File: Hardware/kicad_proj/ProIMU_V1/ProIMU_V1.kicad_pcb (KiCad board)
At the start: 2 copper layers, 50 x 50 mm, 66 parts, among them IC1 MP2731GQC-0000-Z, J1 Conn_02x03_Counter_Clockwise, J4 502570-0893, Q1 2SC4213, U1 ADM101E, U10 STM32F412RETx, U2 TJA1051T-3, U3 LTC2942-1, U4 AIR602, U5 BMP280, U6 MPU-9250, U7 TPS54308, U9 L80-M39

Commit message: Updated Schematic and Layout
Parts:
- C1, C17, C18, C19, C20, C21, C22, C4, U1, U2: moved to F.Cu
- C5, R1, R2: moved to B.Cu
- moved IC1 173.3 mm to (47.5, 85.5)
- moved C12 169.9 mm to (79.1, 88.4)
- moved C26 169.9 mm to (53.7, 97.1)
- moved C6 169.9 mm to (96.4, 57.3)
- moved D2 169.9 mm to (56.4, 87.8)
- moved R14 169.9 mm to (48.8, 101.1)
- moved R15 169.9 mm to (53.4, 93.2)
- moved BAT1 169.9 mm to (49.5, 92.5)
- moved C10 169.9 mm to (86.1, 70.9)
- moved C11 169.9 mm to (94.0, 59.2)
- moved C14 169.9 mm to (75.8, 90.4)
- moved C16 169.9 mm to (124.5, 56.5)
- moved C2 169.9 mm to (76.2, 78.2)
- moved C23 169.9 mm to (56.6, 92.1)
- moved C24 169.9 mm to (60.0, 87.6)
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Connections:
- C5 pad 1: GND -> Net-(CAN1-Pad1)
- CAN1 pad 1: GND -> Net-(CAN1-Pad1)
- CAN1 pad 4: GND -> Net-(CAN1-Pad1)
- U10 pad 11: /MCU/GPS_RESET -> unconnected-(U10-Pad11)
- U10 pad 28: unconnected-(U10-Pad28) -> /MCU/GPS_RESET
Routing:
- net /MCU/CAN_SHUTDOWN: track 0.00 -> 23.5 mm, vias 0 -> 1
- net /MCU/WIFI_UART2_TX: track 0.00 -> 23.3 mm, vias 0 -> 1
- net /MCU/WIFI_UART2_RX: track 0.00 -> 21.9 mm, vias 0 -> 1
- net Net-(CAN1-Pad1): track 0.00 -> 18.7 mm, vias 0 -> 2
- net /MCU/SDCARD_DET_LEVEL: track 0.00 -> 18.2 mm
- net /MCU/GPS_RESET: track 0.00 -> 18.0 mm, vias 0 -> 1
- net /MCU/WIFI_RESET: track 0.00 -> 17.7 mm, vias 0 -> 1
- net /MCU/CAN1_RX: track 0.00 -> 16.6 mm, vias 0 -> 1
- net /MCU/MPU9250_SPI1_nCSS: track 0.00 -> 12.7 mm, vias 0 -> 1
- net /MCU/MPU9250_SPI1_SCK: track 0.00 -> 12.5 mm, vias 0 -> 1
- net /MCU/MPU9250_SPI1_MISO: track 0.00 -> 12.3 mm, vias 0 -> 1
- net /MCU/CAN1_TX: track 0.00 -> 11.5 mm, vias 0 -> 1
- net Net-(C21-Pad2): track 11.5 -> 0.00 mm, vias 2 -> 0
- net /MCU/SDCARD_DET_SWT: track 0.00 -> 8.93 mm
- net /Battery/D+: track 10.5 -> 18.4 mm, vias 3 -> 2
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- removed copper zone on B.Cu, net GND
- removed copper zone on F.Cu, net GND
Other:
- outline, holes or cut-outs redrawn
- board text added: "GND"
- board text added: "NRST"
- board text added: "RX"
- board text added: "SWCLK"
- board text added: "SWDIO"
- board text added: "TX"

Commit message: Updated Schematic and Layout
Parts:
- turned U1 to 180 degrees
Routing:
- net Net-(C21-Pad2): track 0.00 -> 8.73 mm, vias 0 -> 2
- net Net-(RS232-Pad4): track 0.00 -> 8.55 mm
- net Net-(RS232-Pad3): track 0.00 -> 6.15 mm, vias 0 -> 2
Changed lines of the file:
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@@
   )
   (footprint "Package_SO:MSOP-10_3x3mm_P0.5mm" (layer "F.Cu")
-    (at 136 92.7)
+    (at 136 92.7 180)
     (descr "10-Lead Plastic Micro Small Outline Package (MS) [MSOP] (see Microchip Packaging Specification 00000049BS.pdf)")
     (tags "SSOP 0.5")
@@
     (fp_line (start 1.5 -1.5) (end 1.5 1.5) (layer "F.Fab") (width 0.15))
     (fp_line (start -0.5 -1.5) (end 1.5 -1.5) (layer "F.Fab") (width 0.15))
-    (pad "1" smd rect (at -2.2 -1) (size 1.4 0.3) (layers "F.Cu" "F.Paste" "F.Mask")
+    (pad "1" smd rect (at -2.2 -1 180) (size 1.4 0.3) (layers "F.Cu" "F.Paste" "F.Mask")
       (net 37 "GND2") (pinfunction "GND") (pintype "power_in"))
-    (pad "2" smd rect (at -2.2 -0.5) (size 1.4 0.3) (layers "F.Cu" "F.Paste" "F.Mask")
+    (pad "2" smd rect (at -2.2 -0.5 180) (size 1.4 0.3) (layers "F.Cu" "F.Paste" "F.Mask")
       (net 35 "Net-(C4-Pad1)") (pinfunction "C1-") (pintype "passive"))
-    (pad "3" smd rect (at -2.2 0) (size 1.4 0.3) (layers "F.Cu" "F.Paste" "F.Mask")
+    (pad "3" smd rect (at -2.2 0 180) (size 1.4 0.3) (layers "F.Cu" "F.Paste" "F.Mask")
       (net 39 "Net-(C22-Pad2)") (pinfunction "VS-") (pintype "power_out"))
-    (pad "4" smd rect (at -2.2 0.5) (size 1.4 0.3) (layers "F.Cu" "F.Paste" "F.Mask")
+    (pad "4" smd rect (at -2.2 0.5 180) (size 1.4 0.3) (layers "F.Cu" "F.Paste" "F.Mask")
       (net 99 "/MCU/RS232_UART3_TX") (pinfunction "T1IN") (pintype "input"))
-    (pad "5" smd rect (at -2.2 1) (size 1.4 0.3) (layers "F.Cu" "F.Paste" "F.Mask")
+    (pad "5" smd rect (at -2.2 1 180) (size 1.4 0.3) (layers "F.Cu" "F.Paste" "F.Mask")
       (net 41 "Net-(RS232-Pad4)") (pinfunction "R1OUT") (pintype "output"))
-    (pad "6" smd rect (at 2.2 1) (size 1.4 0.3) (layers "F.Cu" "F.Paste" "F.Mask")
+    (pad "6" smd rect (at 2.2 1 180) (size 1.4 0.3) (layers "F.Cu" "F.Paste" "F.Mask")
       (net 90 "/MCU/RS232_UART3_RX") (pinfunction "R1IN") (pintype "input"))
-    (pad "7" smd rect (at 2.2 0.5) (size 1.4 0.3) (layers "F.Cu" "F.Paste" "F.Mask")
+    (pad "7" smd rect (at 2.2 0.5 180) (size 1.4 0.3) (layers "F.Cu" "F.Paste" "F.Mask")
       (net 40 "Net-(RS232-Pad3)") (pinfunction "T1OUT") (pintype "output"))
-    (pad "8" smd rect (at 2.2 0) (size 1.4 0.3) (layers "F.Cu" "F.Paste" "F.Mask")
+    (pad "8" smd rect (at 2.2 0 180) (size 1.4 0.3) (layers "F.Cu" "F.Paste" "F.Mask")
       (net 42 "unconnected-(U1-Pad8)") (pinfunction "SD") (pintype "input+no_connect"))
-    (pad "9" smd rect (at 2.2 -0.5) (size 1.4 0.3) (layers "F.Cu" "F.Paste" "F.Mask")
+    (pad "9" smd rect (at 2.2 -0.5 180) (size 1.4 0.3) (layers "F.Cu" "F.Paste" "F.Mask")
       (net 36 "Net-(C4-Pad2)") (pinfunction "C1+") (pintype "passive"))
-    (pad "10" smd rect (at 2.2 -1) (size 1.4 0.3) (layers "F.Cu" "F.Paste" "F.Mask")
+    (pad "10" smd rect (at 2.2 -1 180) (size 1.4 0.3) (layers "F.Cu" "F.Paste" "F.Mask")
       (net 10 "Net-(C21-Pad2)") (pinfunction "VCC") (pintype "power_in"))
     (model "${KICAD6_3DMODEL_DIR}/Package_SO.3dshapes/MSOP-10_3x3mm_P0.5mm.wrl"
@@
     (effects (font (size 1 1) (thickness 0.15)) (justify mirror))
   )
+  (segment (start 136.5 92.6) (end 136.6 92.5) (width 0.25) (layer "F.Cu") (net 10))
+  (segment (start 133.8 93.7) (end 135.4 93.7) (width 0.25) (layer "F.Cu") (net 10))
+  (segment (start 135.4 93.7) (end 136.5 92.6) (width 0.25) (layer "F.Cu") (net 10))
+  (segment (start 136.6 92.5) (end 136.6 91.6) (width 0.25) (layer "F.Cu") (net 10))
+  (via (at 138.5 87.85) (size 0.8) (drill 0.4) (layers "F.Cu" "B.Cu") (net 10))
+  (via (at 136.6 91.6) (size 0.8) (drill 0.4) (layers "F.Cu" "B.Cu") (net 10))
+  (segment (start 136.6 91.6) (end 136.6 89.75) (width 0.25) (layer "B.Cu") (net 10))
+  (segment (start 136.6 89.75) (end 138.5 87.85) (width 0.25) (layer "B.Cu") (net 10))
   (segment (start 146.886197 113.34952) (end 142.45048 113.34952) (width 0.25) (layer "B.Cu") (net 12))
   (segment (start 147.75 110.675) (end 147.75 112.485718) (width 0.25) (layer "B.Cu") (net 12))
@@
   (via (at 148.5 89.6) (size 0.8) (drill 0.4) (layers "F.Cu" "B.Cu") (net 19))
   (segment (start 148.5 89.5625) (end 148.5 89.6) (width 0.25) (layer "B.Cu") (net 19))
+  (segment (start 134.5 87.9) (end 134.4 88) (width 0.25) (layer "F.Cu") (net 40))
+  (segment (start 134.5 87.85) (end 134.5 87.9) (width 0.25) (layer "F.Cu") (net 40))
+  (segment (start 135.1 92.2) (end 133.8 92.2) (width 0.25) (layer "F.Cu") (net 40))
+  (segment (start 135.3 92) (end 135.1 92.2) (width 0.25) (layer "F.Cu") (net 40))
+  (via (at 134.4 88) (size 0.8) (drill 0.4) (layers "F.Cu" "B.Cu") (net 40))
+  (via (at 135.3 92) (size 0.8) (drill 0.4) (layers "F.Cu" "B.Cu") (net 40))
+  (segment (start 134.4 88) (end 135.3 88.9) (width 0.25) (layer "B.Cu") (net 40))
+  (segment (start 135.3 88.9) (end 135.3 92) (width 0.25) (layer "B.Cu") (net 40))
+  (segment (start 132.5 90) (end 132.5 87.85) (width 0.25) (layer "F.Cu") (net 41))
+  (segment (start 138.2 91.7) (end 137.1 90.6) (width 0.25) (layer "F.Cu") (net 41))
+  (segment (start 137.1 90.6) (end 133.1 90.6) (width 0.25) (layer "F.Cu") (net 41))
+  (segment (start 133.1 90.6) (end 132.5 90) (width 0.25) (layer "F.Cu") (net 41))
   (via (at 154 126) (size 0.8) (drill 0.4) (layers "F.Cu" "B.Cu") (net 61))
   (segment (start 156.7 111.4) (end 156.7 125.7) (width 0.25) (layer "B.Cu") (net 61))

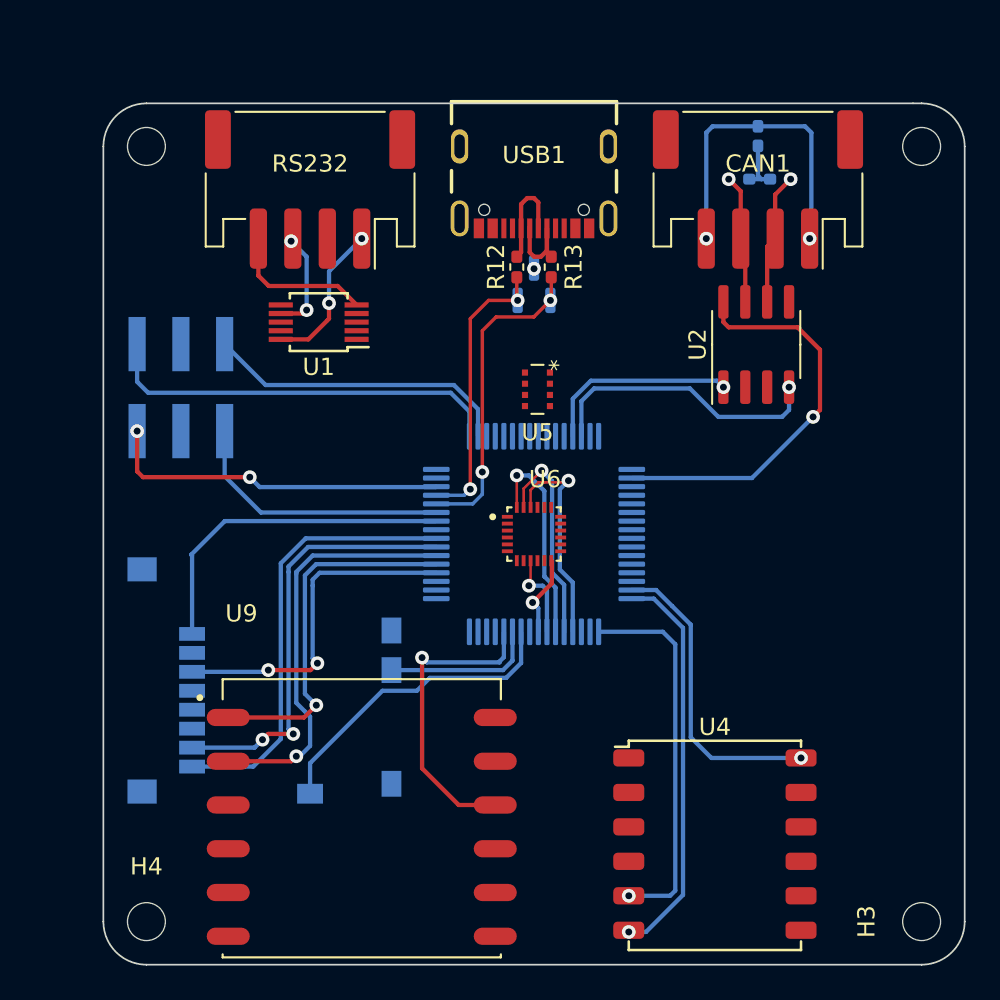
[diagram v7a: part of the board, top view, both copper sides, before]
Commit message: Updated layout
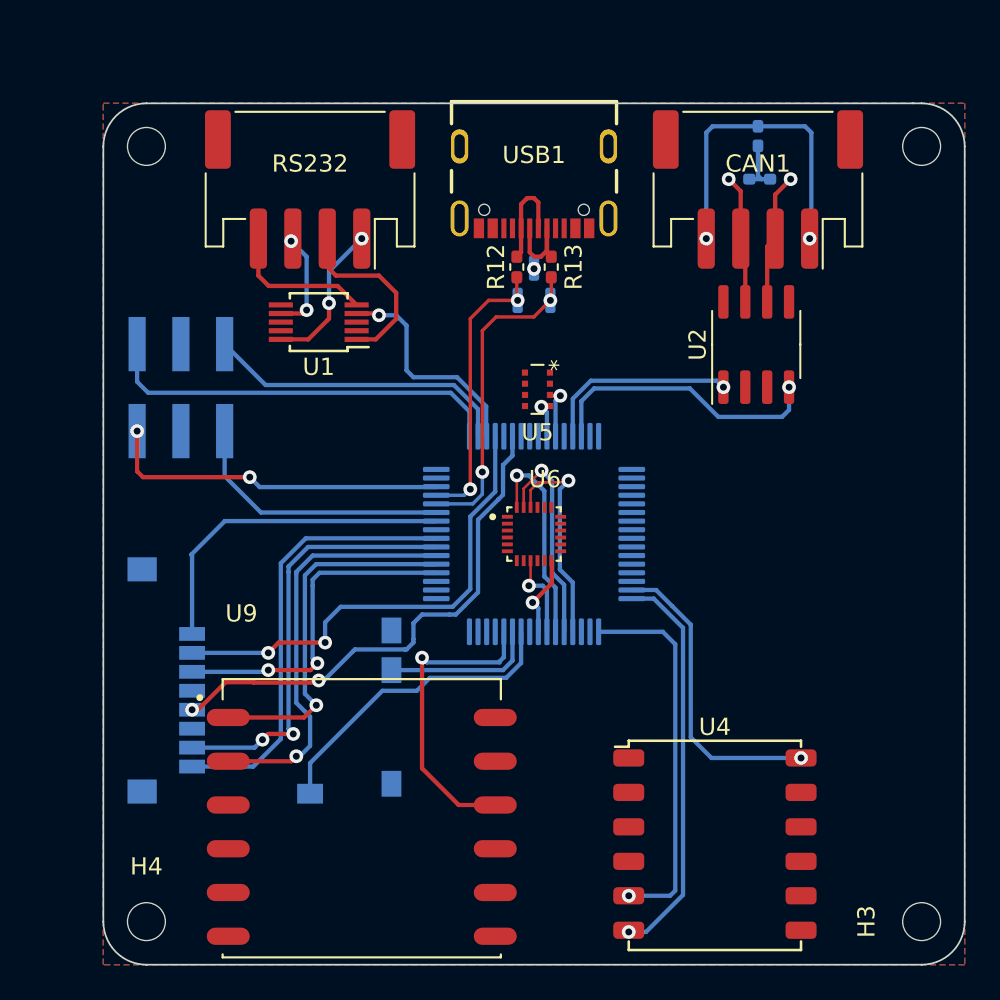
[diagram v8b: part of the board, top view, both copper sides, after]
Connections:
- U10 pad 2: /MCU/CAN_SHUTDOWN -> unconnected-(U10-Pad2)
- U2 pad 8: /MCU/CAN_SHUTDOWN -> GND
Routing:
- net /MCU/SDCARD_SDIO_CMD: track 0.00 -> 30.0 mm, vias 0 -> 2
- net /MCU/SDCARD_SDIO_D3: track 0.00 -> 27.8 mm, vias 0 -> 2
- net /MCU/CAN_SHUTDOWN: track 23.5 -> 0.00 mm, vias 1 -> 0
- net /MCU/RS232_UART3_TX: track 0.00 -> 13.0 mm, vias 0 -> 1
- net GND2: track 0.00 -> 10.6 mm
- net /MCU/BMP280_I2C1_SDA: track 0.00 -> 3.09 mm, vias 0 -> 1
- net /MCU/BMP280_I2C1_SCL: track 0.00 -> 2.36 mm, vias 0 -> 1
- added copper zone on B.Cu, net +3V3
- added copper zone on F.Cu, net GND
